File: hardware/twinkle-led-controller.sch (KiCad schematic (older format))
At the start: 54 parts, among them J1 USB_B_Micro, J10 Screw_Terminal_01x02, J11 Screw_Terminal_01x02, J12 Screw_Terminal_01x02, J2 Conn_01x05, J3 Screw_Terminal_01x02, J4 Screw_Terminal_01x02, J5 Screw_Terminal_01x02, J6 Screw_Terminal_01x02, J7 Screw_Terminal_01x02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

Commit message: Add footprints
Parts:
- removed C10, C11, C12, C13, C14, C15, C16, C17, C8, C9: 0.1uF, symbol Device:C
- removed J10, J11, J12, J3, J4, J5, J6, J7, J8, J9: Screw_Terminal_01x02, symbol Connector:Screw_Terminal_01x02
- removed U10, U11, U12, U13, U4, U5, U6, U7, U8, U9: HT7K1201, symbol homebrew:HT7K1201
- C1: footprint (none) -> Capacitor_SMD:C_0402_1005Metric; LCSC (none) -> C52923
- C2: value C -> 0.1uF; footprint (none) -> Capacitor_SMD:C_0402_1005Metric; LCSC (none) -> C1525
- C3, C5: footprint (none) -> Capacitor_SMD:C_0603_1608Metric; LCSC (none) -> C19666
- C4: footprint (none) -> Capacitor_SMD:C_0603_1608Metric; LCSC (none) -> C59461
- C6: value 10uF -> 22uF; footprint (none) -> Capacitor_SMD:C_0603_1608Metric; LCSC (none) -> C59461
- C7: footprint (none) -> Capacitor_SMD:C_0402_1005Metric; LCSC (none) -> C1525
- D1: footprint (none) -> Diode_SMD:D_SMB; LCSC (none) -> C78395
- D2: footprint (none) -> LED_SMD:LED_0603_1608Metric; LCSC (none) -> C2286
- H1, H2, H3, H4: footprint (none) -> homebrew:HOLE_M4
- J1: footprint (none) -> homebrew:FRAMATOME_10118194-0001LF_fixed_bridges
- J2: footprint (none) -> Connector_PinHeader_2.54mm:PinHeader_1x05_P2.54mm_Vertical
- Q1, Q2: footprint (none) -> Package_TO_SOT_SMD:SOT-23; LCSC (none) -> C2150
- R1, R2, R3: footprint (none) -> Resistor_SMD:R_0402_1005Metric; LCSC (none) -> C25744
- SW1: footprint (none) -> homebrew:SW_TACTILE_5.1MM_TS-1187A-C-D-B; LCSC (none) -> C318888
- U1: footprint (none) -> Package_TO_SOT_SMD:SOT-223; LCSC (none) -> C6186
- U2: LCSC (none) -> C47742
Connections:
- wire segments 131 -> 91

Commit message: Layout v1.0
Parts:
- added R14: 1k, Resistor_SMD:R_0402_1005Metric, symbol Device:R
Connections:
- net GND: now also R14.1; no longer D2.1 (K)
- net LED0_A: now also U3.36 (IO22); no longer U3.26 (IO4)
- net LED0_B: now also U3.37 (IO23); no longer U3.16 (IO13)
- net LED1_A: now also U3.31 (IO19); no longer U3.13 (IO14)
- net LED1_B: now also U3.33 (IO21); no longer U3.27 (IO16)
- net LED3_A: now also U3.26 (IO4); no longer U3.31 (IO19)
- net LED3_B: now also U3.27 (IO16); no longer U3.33 (IO21)
- net LED4_A: now also U3.21 (SDO/SD0); no longer U3.36 (IO22)
- net LED4_B: now also U3.22 (SDI/SD1); no longer U3.37 (IO23)
- net LED5_A: now also U3.18 (SWP/SD3); no longer U3.10 (IO25)
- net LED5_B: now also U3.20 (SCK/CLK); no longer U3.11 (IO26)
- net LED6_A: now also U3.16 (IO13); no longer U3.12 (IO27)
- net LED6_B: now also U3.17 (SHD/SD2); no longer U3.8 (IO32)
- net LED7_A: now also U3.12 (IO27); no longer U3.9 (IO33)
- net LED7_B: now also U3.13 (IO14); no longer U3.21 (SDO/SD0)
- net LED8_A: now also U3.10 (IO25); no longer U3.22 (SDI/SD1)
- net LED8_B: now also U3.11 (IO26); no longer U3.17 (SHD/SD2)
- net LED9_A: now also U3.8 (IO32); no longer U3.18 (SWP/SD3)
- net LED9_B: now also U3.9 (IO33); no longer U3.20 (SCK/CLK)
- new net: D2.1 (K), R14.2
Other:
- moved on the sheet: D2
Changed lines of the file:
@@
 Connection ~ 850  1450
-$Comp
-L Device:D_TVS D1
-U 1 1 5F41F81A
-P 1750 1000
-F 0 "D1" V 1704 1080 50  0000 L CNN
-F 1 "D_TVS" V 1795 1080 50  0000 L CNN
-F 2 "Diode_SMD:D_SMB" H 1750 1000 50  0001 C CNN
-F 3 "~" H 1750 1000 50  0001 C CNN
-F 4 "C78395" V 1750 1000 50  0001 C CNN "LCSC"
-	1    1750 1000
-	0    1    1    0
-$EndComp
-$Comp
-L power:GND #PWR012
-U 1 1 5F420527
-P 1750 1150
-F 0 "#PWR012" H 1750 900 50  0001 C CNN
-F 1 "GND" H 1755 977 50  0000 C CNN
-F 2 "" H 1750 1150 50  0001 C CNN
-F 3 "" H 1750 1150 50  0001 C CNN
-	1    1750 1150
-	1    0    0    -1
-$EndComp
-Connection ~ 1150 850
 $Comp
 L Regulator_Linear:AZ1117-3.3 U1
@@
 NoConn ~ 5600 1600
 NoConn ~ 5600 1900
-Text Label 5650 1800 0    50   ~ 0
+Text Label 5650 2900 0    50   ~ 0
 LED0_A
 Wire Wire Line
 	5650 1800 5600 1800
-Text Label 5650 2100 0    50   ~ 0
+Text Label 5650 3000 0    50   ~ 0
 LED0_B
 Wire Wire Line
 	5650 2100 5600 2100
-Text Label 5650 2200 0    50   ~ 0
+Text Label 5650 2700 0    50   ~ 0
 LED1_A
 Wire Wire Line
 	5650 2200 5600 2200
-Text Label 5650 2400 0    50   ~ 0
-LED1_B
 Wire Wire Line
 	5650 2400 5600 2400
@@
 Wire Wire Line
 	5650 2500 5600 2500
-Text Label 5650 2600 0    50   ~ 0
-LED2_B
 Wire Wire Line
 	5650 2600 5600 2600
-Text Label 5650 2700 0    50   ~ 0
+Text Label 5650 1800 0    50   ~ 0
 LED3_A
 Wire Wire Line
 	5650 2700 5600 2700
-Text Label 5650 2800 0    50   ~ 0
+Text Label 5650 2400 0    50   ~ 0
 LED3_B
 Wire Wire Line
 	5650 2800 5600 2800
-Text Label 5650 2900 0    50   ~ 0
-LED4_A
 Wire Wire Line
 	5650 2900 5600 2900
-Text Label 5650 3000 0    50   ~ 0
+Text Label 4350 2700 2    50   ~ 0
 LED4_B
 Wire Wire Line
 	5650 3000 5600 3000
+Text Label 4350 2900 2    50   ~ 0
+LED5_A
+Wire Wire Line
+	5650 3100 5600 3100
+Text Label 4350 3000 2    50   ~ 0
+LED5_B
+Wire Wire Line
+	5650 3200 5600 3200
+Text Label 5650 2100 0    50   ~ 0
+LED6_A
+Wire Wire Line
+	5650 3300 5600 3300
+Text Label 4350 2800 2    50   ~ 0
+LED6_B
+Wire Wire Line
+	5650 3400 5600 3400
+Text Label 5650 3300 0    50   ~ 0
+LED7_A
+Wire Wire Line
+	5650 3500 5600 3500
+Text Label 5650 2200 0    50   ~ 0
+LED7_B
 Text Label 5650 3100 0    50   ~ 0
-LED5_A
-Wire Wire Line
-	5650 3100 5600 3100
+LED8_A
 Text Label 5650 3200 0    50   ~ 0
-LED5_B
-Wire Wire Line
-	5650 3200 5600 3200
-Text Label 5650 3300 0    50   ~ 0
-LED6_A
-Wire Wire Line
-	5650 3300 5600 3300
+LED8_B
+Wire Wire Line
+	4350 2600 4400 2600
 Text Label 5650 3400 0    50   ~ 0
-LED6_B
-Wire Wire Line
-	5650 3400 5600 3400
+LED9_A
+Wire Wire Line
+	4350 2700 4400 2700
 Text Label 5650 3500 0    50   ~ 0
-LED7_A
-Wire Wire Line
-	5650 3500 5600 3500
-Text Label 4350 2600 2    50   ~ 0
-LED7_B
-Text Label 4350 2700 2    50   ~ 0
-LED8_A
-Text Label 4350 2800 2    50   ~ 0
-LED8_B
-Wire Wire Line
-	4350 2600 4400 2600
-Text Label 4350 2900 2    50   ~ 0
-LED9_A
-Wire Wire Line
-	4350 2700 4400 2700
-Text Label 4350 3000 2    50   ~ 0
 LED9_B
 Wire Wire Line
@@
 L Device:LED D2
 U 1 1 5F464E73
-P 3800 4900
-F 0 "D2" V 3839 4782 50  0000 R CNN
-F 1 "LED" V 3748 4782 50  0000 R CNN
-F 2 "LED_SMD:LED_0603_1608Metric" H 3800 4900 50  0001 C CNN
-F 3 "~" H 3800 4900 50  0001 C CNN
-F 4 "C2286" V 3800 4900 50  0001 C CNN "LCSC"
-	1    3800 4900
+P 3800 4550
+F 0 "D2" V 3839 4432 50  0000 R CNN
+F 1 "LED" V 3748 4432 50  0000 R CNN
+F 2 "LED_SMD:LED_0603_1608Metric" H 3800 4550 50  0001 C CNN
+F 3 "~" H 3800 4550 50  0001 C CNN
+F 4 "C2286" V 3800 4550 50  0001 C CNN "LCSC"
+	1    3800 4550
 	0    -1   -1   0
 $EndComp
-Text Label 3800 4750 2    50   ~ 0
+Text Label 3800 4400 2    50   ~ 0
 LED_BUILTIN
 $Comp
 L power:GND #PWR015
 U 1 1 5F4659BC
-P 3800 5150
-F 0 "#PWR015" H 3800 4900 50  0001 C CNN
-F 1 "GND" H 3805 4977 50  0000 C CNN
-F 2 "" H 3800 5150 50  0001 C CNN
-F 3 "" H 3800 5150 50  0001 C CNN
-	1    3800 5150
-	1    0    0    -1
-$EndComp
-Wire Wire Line
-	3800 5150 3800 5050
+P 3800 5100
+F 0 "#PWR015" H 3800 4850 50  0001 C CNN
+F 1 "GND" H 3805 4927 50  0000 C CNN
+F 2 "" H 3800 5100 50  0001 C CNN
+F 3 "" H 3800 5100 50  0001 C CNN
+	1    3800 5100
+	1    0    0    -1
+$EndComp
+Wire Wire Line
+	3800 4800 3800 4700
 Text Label 4350 1600 2    50   ~ 0
 AUX0
@@
 Wire Wire Line
 	4300 5850 4000 5850
-Wire Wire Line
-	1150 850  1750 850
 Wire Wire Line
 	4350 2900 4400 2900
@@
 Wire Wire Line
 	9000 4600 9100 4600
+Text Label 4350 2600 2    50   ~ 0
+LED4_A
+$Comp
+L Device:R R14
+U 1 1 5F43CA52
+P 3800 4950
+F 0 "R14" V 3593 4950 50  0000 C CNN
+F 1 "1k" V 3684 4950 50  0000 C CNN
+F 2 "Resistor_SMD:R_0402_1005Metric" V 3730 4950 50  0001 C CNN
+F 3 "~" H 3800 4950 50  0001 C CNN
+F 4 "C11702" V 3800 4950 50  0001 C CNN "LCSC"
+	1    3800 4950
+	-1   0    0    1
+$EndComp
+Text Label 5650 2600 0    50   ~ 0
+LED2_B
+Text Label 5650 2800 0    50   ~ 0
+LED1_B
+$Comp
+L Device:D_TVS D1
+U 1 1 5F490FDA
+P 1750 1000
+F 0 "D1" V 1704 1079 50  0000 L CNN
+F 1 "D_TVS" V 1795 1079 50  0000 L CNN
+F 2 "Diode_SMD:D_SMB" H 1750 1000 50  0001 C CNN
+F 3 "~" H 1750 1000 50  0001 C CNN
+F 4 "C78395" V 1750 1000 50  0001 C CNN "LCSC"
+	1    1750 1000
+	0    1    1    0
+$EndComp
+Wire Wire Line
+	1750 850  1150 850
+Connection ~ 1150 850
+$Comp
+L power:GND #PWR0101
+U 1 1 5F495F62
+P 1750 1150
+F 0 "#PWR0101" H 1750 900 50  0001 C CNN
+F 1 "GND" H 1755 977 50  0000 C CNN
+F 2 "" H 1750 1150 50  0001 C CNN
+F 3 "" H 1750 1150 50  0001 C CNN
+	1    1750 1150
+	1    0    0    -1
+$EndComp
 $EndSCHEMATC

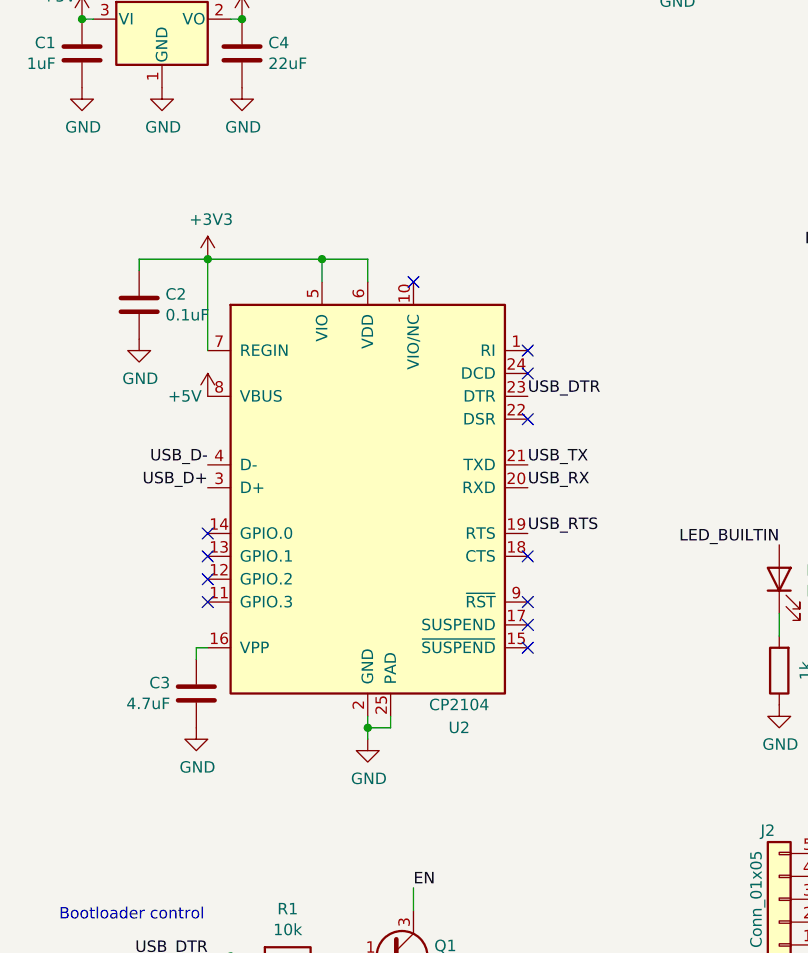
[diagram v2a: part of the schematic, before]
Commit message: Fix v1.0 layout and generate gerbers/placement files
- Update to CP2102, since JLCPCB doesn't have CP2104
- Fix current-limiting resistors to 10 ohm
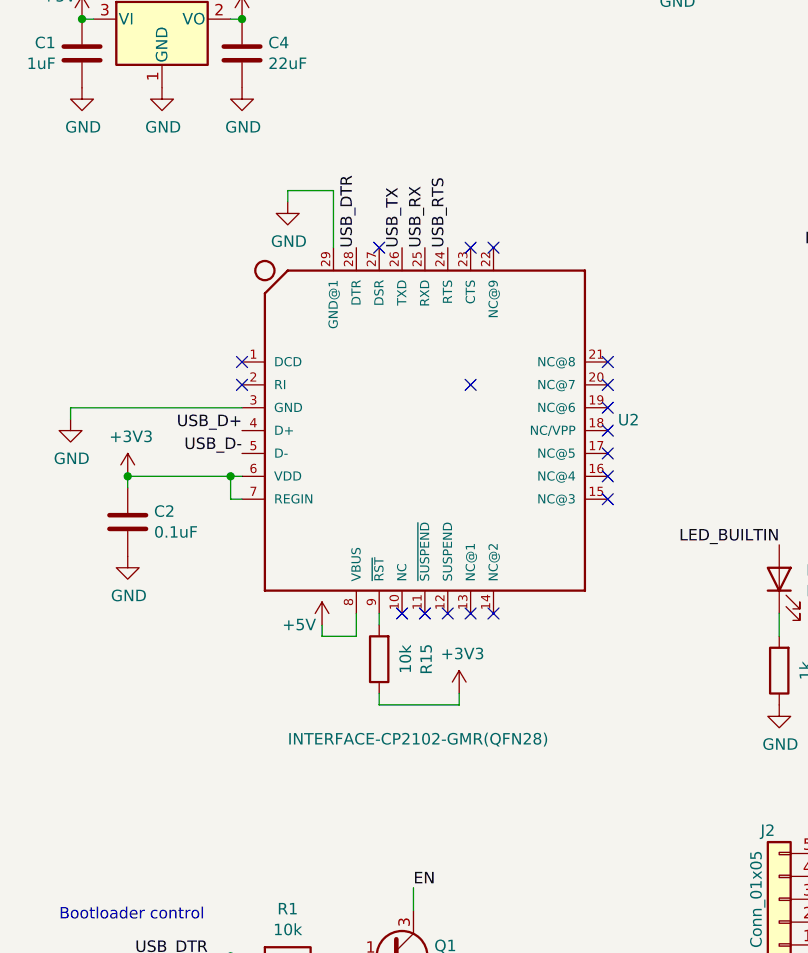
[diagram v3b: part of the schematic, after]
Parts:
- removed C3: 4.7uF, Capacitor_SMD:C_0603_1608Metric, symbol Device:C
- removed U2: CP2104, Package_DFN_QFN:QFN-24-1EP_4x4mm_P0.5mm_EP2.6x2.6mm, symbol Interface_USB:CP2104
- added R15: 10k, Resistor_SMD:R_0402_1005Metric, symbol Device:R
- added U2: INTERFACE-CP2102-GMR(QFN28), snapeda:QFN28G_0.5-5X5MM, symbol snapeda-CP2102:INTERFACE-CP2102-GMR(QFN28)
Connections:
- net +3V3: now also R15.1, U2.6 (VDD), U2.7 (REGIN)
- net +5V: now also U2.8 (VBUS)
- net GND: now also U2.29 (GND@1), U2.3 (GND)
- net USB_D+: now also U2.4 (D+)
- net USB_D-: now also U2.5 (D-)
- net USB_DTR: now also U2.28 (DTR)
- net USB_RTS: now also U2.24 (RTS)
- net USB_RX: now also U2.25 (RXD)
- net USB_TX: now also U2.26 (TXD)
- new net: R15.2, U2.9 (~RST~)
- no-connect marks 19 -> 25
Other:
- moved on the sheet: C2
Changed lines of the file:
@@
-$EndComp
-$Comp
-L Interface_USB:CP2104 U2
-U 1 1 5F42614D
-P 2000 4150
-F 0 "U2" H 2400 3100 50  0000 C CNN
-F 1 "CP2104" H 2400 3200 50  0000 C CNN
-F 2 "Package_DFN_QFN:QFN-24-1EP_4x4mm_P0.5mm_EP2.6x2.6mm" H 2150 3200 50  0001 L CNN
-F 3 "https://www.silabs.com/documents/public/data-sheets/cp2104.pdf" H 1450 5400 50  0001 C CNN
-F 4 "C47742" H 2000 4150 50  0001 C CNN "LCSC"
-	1    2000 4150
-	1    0    0    -1
 $EndComp
 $Comp
 L Device:C C2
 U 1 1 5F42C06B
-P 1000 3350
-F 0 "C2" H 1115 3396 50  0000 L CNN
-F 1 "0.1uF" H 1115 3305 50  0000 L CNN
-F 2 "Capacitor_SMD:C_0402_1005Metric" H 1038 3200 50  0001 C CNN
-F 3 "~" H 1000 3350 50  0001 C CNN
-F 4 "C1525" H 1000 3350 50  0001 C CNN "LCSC"
-	1    1000 3350
-	1    0    0    -1
-$EndComp
-$Comp
-L power:+3V3 #PWR08
-U 1 1 5F42CB84
-P 1300 3150
-F 0 "#PWR08" H 1300 3000 50  0001 C CNN
-F 1 "+3V3" H 1315 3323 50  0000 C CNN
-F 2 "" H 1300 3150 50  0001 C CNN
-F 3 "" H 1300 3150 50  0001 C CNN
-	1    1300 3150
-	1    0    0    -1
-$EndComp
-Wire Wire Line
-	1300 3150 1000 3150
-Wire Wire Line
-	1000 3150 1000 3200
-Wire Wire Line
-	1300 3150 1300 3550
-Connection ~ 1300 3150
-Wire Wire Line
-	1300 3150 1800 3150
-Wire Wire Line
-	1800 3150 1800 3250
-Wire Wire Line
-	1800 3150 2000 3150
-Wire Wire Line
-	2000 3150 2000 3250
-Connection ~ 1800 3150
+P 950 4300
+F 0 "C2" H 1065 4346 50  0000 L CNN
+F 1 "0.1uF" H 1065 4255 50  0000 L CNN
+F 2 "Capacitor_SMD:C_0402_1005Metric" H 988 4150 50  0001 C CNN
+F 3 "~" H 950 4300 50  0001 C CNN
+F 4 "C1525" H 950 4300 50  0001 C CNN "LCSC"
+	1    950  4300
+	1    0    0    -1
+$EndComp
 $Comp
 L power:GND #PWR04
 U 1 1 5F42EA2A
-P 1000 3500
-F 0 "#PWR04" H 1000 3250 50  0001 C CNN
-F 1 "GND" H 1005 3327 50  0000 C CNN
-F 2 "" H 1000 3500 50  0001 C CNN
-F 3 "" H 1000 3500 50  0001 C CNN
-	1    1000 3500
+P 950 4450
+F 0 "#PWR04" H 950 4200 50  0001 C CNN
+F 1 "GND" H 955 4277 50  0000 C CNN
+F 2 "" H 950 4450 50  0001 C CNN
+F 3 "" H 950 4450 50  0001 C CNN
+	1    950  4450
 	1    0    0    -1
 $EndComp
@@
 L power:+5V #PWR09
 U 1 1 5F42EEEA
-P 1300 3750
-F 0 "#PWR09" H 1300 3600 50  0001 C CNN
-F 1 "+5V" H 1200 3750 50  0000 C CNN
-F 2 "" H 1300 3750 50  0001 C CNN
-F 3 "" H 1300 3750 50  0001 C CNN
-	1    1300 3750
-	1    0    0    -1
-$EndComp
-NoConn ~ 2200 3250
-Text Label 1300 4050 2    50   ~ 0
+P 1800 4750
+F 0 "#PWR09" H 1800 4600 50  0001 C CNN
+F 1 "+5V" H 1700 4750 50  0000 C CNN
+F 2 "" H 1800 4750 50  0001 C CNN
+F 3 "" H 1800 4750 50  0001 C CNN
+	1    1800 4750
+	1    0    0    -1
+$EndComp
+Text Label 1450 4000 2    50   ~ 0
 USB_D-
-Text Label 1300 4150 2    50   ~ 0
+Text Label 1450 3900 2    50   ~ 0
 USB_D+
-$Comp
-L Device:C C3
-U 1 1 5F42FFDF
-P 1250 5050
-F 0 "C3" H 1136 5004 50  0000 R CNN
-F 1 "4.7uF" H 1136 5095 50  0000 R CNN
-F 2 "Capacitor_SMD:C_0603_1608Metric" H 1288 4900 50  0001 C CNN
-F 3 "~" H 1250 5050 50  0001 C CNN
-F 4 "C19666" H 1250 5050 50  0001 C CNN "LCSC"
-	1    1250 5050
-	1    0    0    1
-$EndComp
-Wire Wire Line
-	1300 4850 1250 4850
-Wire Wire Line
-	1250 4850 1250 4900
-$Comp
-L power:GND #PWR07
-U 1 1 5F4306E7
-P 1250 5200
-F 0 "#PWR07" H 1250 4950 50  0001 C CNN
-F 1 "GND" H 1255 5027 50  0000 C CNN
-F 2 "" H 1250 5200 50  0001 C CNN
-F 3 "" H 1250 5200 50  0001 C CNN
-	1    1250 5200
-	1    0    0    -1
-$EndComp
-$Comp
-L power:GND #PWR013
-U 1 1 5F430821
-P 2000 5250
-F 0 "#PWR013" H 2000 5000 50  0001 C CNN
-F 1 "GND" H 2005 5077 50  0000 C CNN
-F 2 "" H 2000 5250 50  0001 C CNN
-F 3 "" H 2000 5250 50  0001 C CNN
-	1    2000 5250
-	1    0    0    -1
-$EndComp
-Wire Wire Line
-	2000 5150 2000 5200
-Wire Wire Line
-	2000 5200 2100 5200
-Wire Wire Line
-	2100 5200 2100 5150
-Connection ~ 2000 5200
-Wire Wire Line
-	2000 5200 2000 5250
-NoConn ~ 1300 4350
-NoConn ~ 1300 4450
-NoConn ~ 1300 4550
-NoConn ~ 1300 4650
-NoConn ~ 2700 4650
-NoConn ~ 2700 4750
-NoConn ~ 2700 4850
-NoConn ~ 2700 4450
-Text Label 2700 4350 0    50   ~ 0
+Text Label 2350 3100 1    50   ~ 0
 USB_RTS
-Text Label 2700 4150 0    50   ~ 0
+Text Label 2250 3100 1    50   ~ 0
 USB_RX
-Text Label 2700 4050 0    50   ~ 0
+Text Label 2150 3100 1    50   ~ 0
 USB_TX
-NoConn ~ 2700 3850
-NoConn ~ 2700 3650
-NoConn ~ 2700 3550
-Text Label 2700 3750 0    50   ~ 0
+Text Label 1950 3100 1    50   ~ 0
 USB_DTR
 $Comp
@@
 	1    0    0    -1
 $EndComp
+$Comp
+L snapeda-CP2102:INTERFACE-CP2102-GMR(QFN28) U2
+U 1 1 5F4A17F8
+P 2250 3900
+F 0 "U2" H 3094 3946 50  0000 L CNN
+F 1 "INTERFACE-CP2102-GMR(QFN28)" H 1650 2550 50  0000 L CNN
+F 2 "snapeda:QFN28G_0.5-5X5MM" H 2250 3900 50  0001 L BNN
+F 3 "CP2102-GMR" H 2250 3900 50  0001 L BNN
+F 4 "C6568" H 2250 3900 50  0001 C CNN "LCSC"
+	1    2250 3900
+	1    0    0    -1
+$EndComp
+$Comp
+L power:+3V3 #PWR0103
+U 1 1 5F4AF9EB
+P 950 4100
+F 0 "#PWR0103" H 950 3950 50  0001 C CNN
+F 1 "+3V3" H 965 4273 50  0000 C CNN
+F 2 "" H 950 4100 50  0001 C CNN
+F 3 "" H 950 4100 50  0001 C CNN
+	1    950  4100
+	1    0    0    -1
+$EndComp
+Wire Wire Line
+	950  4100 1400 4100
+Wire Wire Line
+	1400 4100 1400 4200
+Wire Wire Line
+	1400 4200 1450 4200
+Connection ~ 1400 4100
+Wire Wire Line
+	1400 4100 1450 4100
+Wire Wire Line
+	950  4150 950  4100
+Connection ~ 950  4100
+$Comp
+L power:GND #PWR0104
+U 1 1 5F4ECE71
+P 1650 2900
+F 0 "#PWR0104" H 1650 2650 50  0001 C CNN
+F 1 "GND" H 1655 2727 50  0000 C CNN
+F 2 "" H 1650 2900 50  0001 C CNN
+F 3 "" H 1650 2900 50  0001 C CNN
+	1    1650 2900
+	1    0    0    -1
+$EndComp
+Wire Wire Line
+	1850 3100 1850 2850
+Wire Wire Line
+	1850 2850 1650 2850
+Wire Wire Line
+	1650 2850 1650 2900
+Wire Wire Line
+	1800 4750 1800 4800
+Wire Wire Line
+	1800 4800 1950 4800
+Wire Wire Line
+	1950 4700 1950 4800
+$Comp
+L power:GND #PWR0105
+U 1 1 5F4F952B
+P 700 3850
+F 0 "#PWR0105" H 700 3600 50  0001 C CNN
+F 1 "GND" H 705 3677 50  0000 C CNN
+F 2 "" H 700 3850 50  0001 C CNN
+F 3 "" H 700 3850 50  0001 C CNN
+	1    700  3850
+	1    0    0    -1
+$EndComp
+Wire Wire Line
+	700  3800 1450 3800
+Wire Wire Line
+	700  3850 700  3800
+$Comp
+L Device:R R15
+U 1 1 5F502C4A
+P 2050 4900
+F 0 "R15" V 1843 4900 50  0000 C CNN
+F 1 "10k" V 1934 4900 50  0000 C CNN
+F 2 "Resistor_SMD:R_0402_1005Metric" V 1980 4900 50  0001 C CNN
+F 3 "~" H 2050 4900 50  0001 C CNN
+F 4 "C25744" V 2050 4900 50  0001 C CNN "LCSC"
+	1    2050 4900
+	-1   0    0    1
+$EndComp
+$Comp
+L power:+3V3 #PWR0106
+U 1 1 5F504FBE
+P 2400 5050
+F 0 "#PWR0106" H 2400 4900 50  0001 C CNN
+F 1 "+3V3" H 2415 5223 50  0000 C CNN
+F 2 "" H 2400 5050 50  0001 C CNN
+F 3 "" H 2400 5050 50  0001 C CNN
+	1    2400 5050
+	1    0    0    -1
+$EndComp
+Wire Wire Line
+	2050 5050 2050 5100
+Wire Wire Line
+	2050 5100 2400 5100
+Wire Wire Line
+	2400 5100 2400 5050
+Wire Wire Line
+	2050 4750 2050 4700
+NoConn ~ 2150 4700
+NoConn ~ 2250 4700
+NoConn ~ 2350 4700
+NoConn ~ 2450 4700
+NoConn ~ 2550 4700
+NoConn ~ 3050 4200
+NoConn ~ 3050 4100
+NoConn ~ 3050 4000
+NoConn ~ 3050 3900
+NoConn ~ 3050 3800
+NoConn ~ 3050 3700
+NoConn ~ 3050 3600
+NoConn ~ 1450 3700
+NoConn ~ 1450 3600
+NoConn ~ 2450 3100
+NoConn ~ 2550 3100
+NoConn ~ 2050 3100
+NoConn ~ 2450 3700
 $EndSCHEMATC
